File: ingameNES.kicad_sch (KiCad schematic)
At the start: 6 parts, among them J1 SJ-43504-SMT-TR

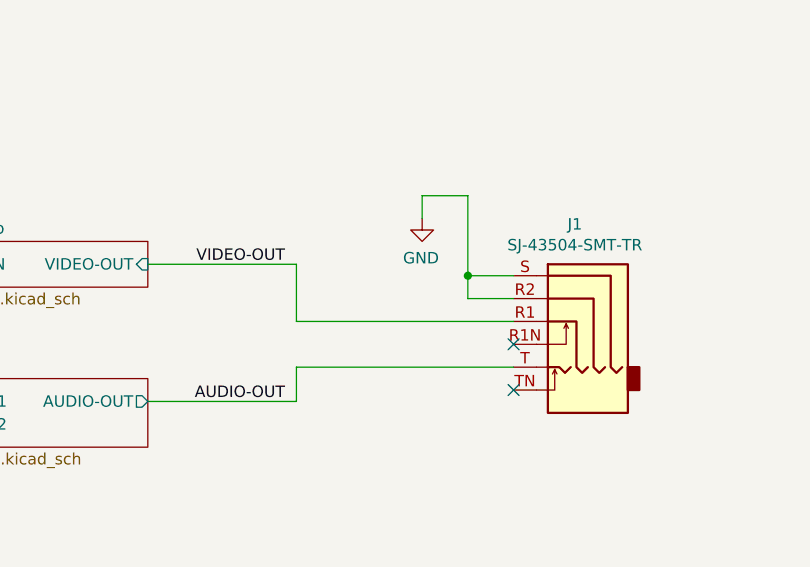
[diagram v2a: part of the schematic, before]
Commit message: InGameNES rev 2.1
Change AV pinout to CTIA standard. Mono audio goes to R and L channels. Video now pinned to sleeve so its yellow on 3RCA breakout.
-Added boundary rule so copper fills do not bridge pins. The bridges were on SRAM near capacitors. It is electrically correct but it looks wrong for QA.
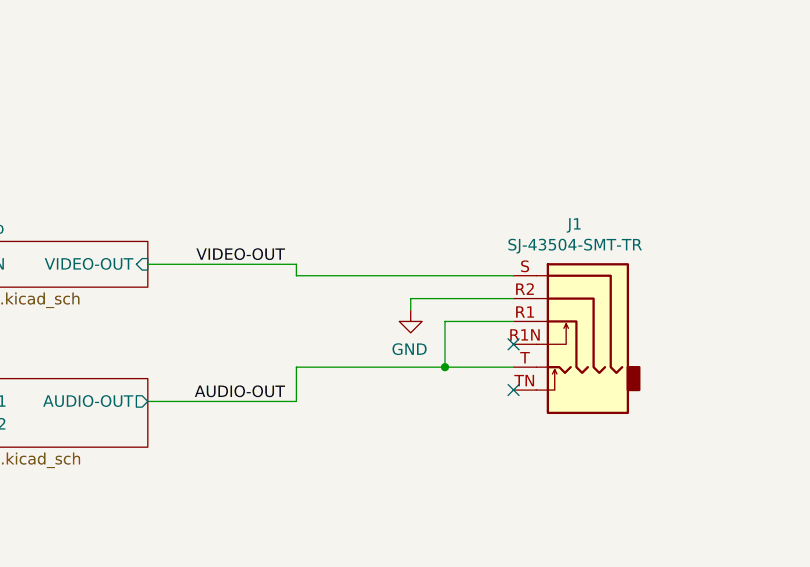
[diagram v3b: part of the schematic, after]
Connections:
- net AUDIO-OUT: now also J1.R1
- net GND: no longer J1.S
- net VIDEO-OUT: now also J1.S; no longer J1.R1
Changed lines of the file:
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@@
   (title_block
     (title "InGame-NES MMC3")
-    (date "2022-08-02")
-    (rev "2")
+    (date "2022-08-10")
+    (rev "2.1")
     (company "Late to the Game")
   )
   (junction (at 123.19 81.28) (diameter 0) (color 0 0 0 0)
   )
-  (junction (at 238.76 118.11) (diameter 0) (color 0 0 0 0)
-  )
   (junction (at 106.68 68.58) (diameter 0) (color 0 0 0 0)
   )
   (junction (at 120.65 68.58) (diameter 0) (color 0 0 0 0)
+  )
+  (junction (at 236.22 128.27) (diameter 0) (color 0 0 0 0)
   )
   (no_connect (at 243.84 130.81))
   (no_connect (at 243.84 125.73))
-  (wire (pts (xy 243.84 118.11) (xy 238.76 118.11))
+  (wire (pts (xy 243.84 123.19) (xy 236.22 123.19))
     (stroke (width 0) (type default) (color 0 0 0 0))
   )
@@
     (stroke (width 0) (type default) (color 0 0 0 0))
   )
-  (wire (pts (xy 243.84 120.65) (xy 238.76 120.65))
-    (stroke (width 0) (type default) (color 0 0 0 0))
-  )
   (polyline (pts (xy -43.18 200.66) (xy -43.18 250.19))
     (stroke (width 0) (type default) (color 0 0 0 0))
@@
     (stroke (width 0) (type default) (color 0 0 0 0))
   )
+  (wire (pts (xy 236.22 128.27) (xy 243.84 128.27))
+    (stroke (width 0) (type default) (color 0 0 0 0))
+  )
   (wire (pts (xy 121.92 26.67) (xy 115.57 26.67))
     (stroke (width 0) (type default) (color 0 0 0 0))
   )
-  (wire (pts (xy 238.76 120.65) (xy 238.76 118.11))
-    (stroke (width 0) (type default) (color 0 0 0 0))
-  )
   (wire (pts (xy 67.31 81.28) (xy 123.19 81.28))
     (stroke (width 0) (type default) (color 0 0 0 0))
@@
     (stroke (width 0) (type default) (color 0 0 0 0))
   )
-  (wire (pts (xy 238.76 118.11) (xy 238.76 109.22))
-    (stroke (width 0) (type default) (color 0 0 0 0))
-  )
-  (wire (pts (xy 233.68 109.22) (xy 233.68 111.76))
+  (wire (pts (xy 243.84 118.11) (xy 219.71 118.11))
+    (stroke (width 0) (type default) (color 0 0 0 0))
+  )
+  (wire (pts (xy 232.41 120.65) (xy 232.41 121.92))
     (stroke (width 0) (type default) (color 0 0 0 0))
   )
@@
     (stroke (width 0) (type default) (color 0 0 0 0))
   )
-  (wire (pts (xy 219.71 128.27) (xy 243.84 128.27))
-    (stroke (width 0) (type default) (color 0 0 0 0))
-  )
   (wire (pts (xy 67.31 91.44) (xy 85.09 91.44))
     (stroke (width 0) (type default) (color 0 0 0 0))
@@
     (stroke (width 0) (type default) (color 0 0 0 0))
   )
+  (wire (pts (xy 236.22 123.19) (xy 236.22 128.27))
+    (stroke (width 0) (type default) (color 0 0 0 0))
+  )
   (wire (pts (xy 219.71 128.27) (xy 219.71 132.08))
     (stroke (width 0) (type default) (color 0 0 0 0))
@@
     (stroke (width 0) (type default) (color 0 0 0 0))
   )
-  (wire (pts (xy 243.84 123.19) (xy 219.71 123.19))
-    (stroke (width 0) (type default) (color 0 0 0 0))
-  )
   (bus (pts (xy 118.11 93.98) (xy 135.89 93.98))
     (stroke (width 0) (type default) (color 0 0 0 0))
@@
     (stroke (width 0) (type default) (color 0 0 0 0))
   )
+  (wire (pts (xy 219.71 128.27) (xy 236.22 128.27))
+    (stroke (width 0) (type default) (color 0 0 0 0))
+  )
   (polyline (pts (xy -43.18 250.19) (xy -83.82 250.19))
     (stroke (width 0) (type default) (color 0 0 0 0))
   )
-  (wire (pts (xy 219.71 116.84) (xy 219.71 123.19))
+  (wire (pts (xy 219.71 116.84) (xy 219.71 118.11))
     (stroke (width 0) (type default) (color 0 0 0 0))
   )
@@
     (stroke (width 0) (type default) (color 0 0 0 0))
   )
-  (wire (pts (xy 238.76 109.22) (xy 233.68 109.22))
+  (wire (pts (xy 232.41 120.65) (xy 243.84 120.65))
     (stroke (width 0) (type default) (color 0 0 0 0))
   )
@@
     (pin "TN")
   )
-  (symbol (lib_id "power:GND") (at 233.68 111.76 0) (mirror y) (unit 1)
+  (symbol (lib_id "power:GND") (at 232.41 121.92 0) (mirror y) (unit 1)
     (in_bom yes) (on_board yes)
-    (property "Reference" "#PWR0164" (id 0) (at 233.68 118.11 0)
-      (effects (font (size 1.27 1.27)) hide)
-    )
-    (property "Value" "GND" (id 1) (at 233.553 116.1542 0))
-    (property "Footprint" "" (id 2) (at 233.68 111.76 0)
-      (effects (font (size 1.27 1.27)) hide)
-    )
-    (property "Datasheet" "" (id 3) (at 233.68 111.76 0)
-      (effects (font (size 1.27 1.27)) hide)
-    )
+    (property "Reference" "#PWR0164" (id 0) (at 232.41 128.27 0)
+      (effects (font (size 1.27 1.27)) hide)
+    )
+    (property "Value" "GND" (id 1) (at 232.283 126.3142 0))
+    (property "Footprint" "" (id 2) (at 232.41 121.92 0)
+      (effects (font (size 1.27 1.27)) hide)
+    )
+    (property "Datasheet" "" (id 3) (at 232.41 121.92 0)
+      (effects (font (size 1.27 1.27)) hide)
+    )
